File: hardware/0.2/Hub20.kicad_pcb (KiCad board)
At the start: 2 copper layers, 89 x 124 mm, 164 parts, among them J1 USB_C_Receptacle_USB2.0, J2 USB_C_Receptacle_USB2.0, J3 USB_C_Receptacle_USB2.0, J4 USB_C_Receptacle_USB2.0, Q1 DTC123J, Q2 BSS138, SW1 SW_Push, SW10 MX_RGB, SW11 MX_RGB, SW12 MX_RGB, SW13 Rotary_Encoder_Switch, SW14 MX_RGB, SW15 MX_RGB, SW16 MX_RGB, SW17 MX_RGB, SW18 MX_RGB, SW19 MX_RGB, SW2 MX_RGB, SW20 MX_RGB, SW21 MX_RGB, SW22 MX_RGB, SW23 MX_RGB, SW3 MX_RGB, SW4 MX_RGB, SW5 MX_RGB, SW6 MX_RGB, SW7 Rotary_Encoder_Switch, SW8 MX_RGB, SW9 MX_RGB, U1 AP2112K-3.3, U2 USBLC6-2SC6, U3 STM32F072C8Tx, U5 CY7C65632-28LTXCT, U6 USBLC6-2SC6, U7 USBLC6-2SC6, U8 USBLC6-2SC6, Y1 12MHz

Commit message: layout getting close
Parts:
- moved R6 53.2 mm to (163.4, 114.7), turned to 0 degrees
- moved Q2 49.7 mm to (163.4, 112.2), turned to 270 degrees
- moved R5 46.2 mm to (163.4, 109.7), turned to 0 degrees
- moved C9 1.05 mm to (123.8, 70.5), turned to 270 degrees
- moved D24 0.80 mm to (160.9, 43.1)
- moved C38 0.70 mm to (144.5, 86.2)
- moved R10 0.27 mm to (151.9, 51.1)
- moved C59 0.10 mm to (146.7, 42.6)
- moved F3 0.10 mm to (146.5, 44.3)
- moved FB4 0.10 mm to (146.3, 46.0)
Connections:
- C41 pad 1: +3V3 -> +3.3VP
- C56 pad 1: +3V3 -> +3.3VP
- C57 pad 1: +3V3 -> +3.3VP
- FB2 pad 2: +3V3 -> +3.3VP
- R8 pad 2: +3V3 -> +3.3VP
- R9 pad 2: +3V3 -> +3.3VP
- RN3 pad 5: +3V3 -> +3.3VP
- RN3 pad 6: +3V3 -> +3.3VP
- RN3 pad 7: +3V3 -> +3.3VP
- RN3 pad 8: +3V3 -> +3.3VP
- U5 pad 21: +3V3 -> +3.3VP
- U5 pad 28: +3V3 -> +3.3VP
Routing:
- net +3V3: track 22.1 -> 300.4 mm, vias 0 -> 24
- net /C1: track 0.00 -> 190.8 mm, vias 0 -> 8
- net /C2: track 0.00 -> 181.4 mm, vias 0 -> 4
- net /C0: track 0.00 -> 126.5 mm, vias 0 -> 3
- net /C3: track 0.00 -> 117.2 mm, vias 0 -> 7
- net Net-(R1-Pad2): track 0.00 -> 115.7 mm, vias 0 -> 6
- net /R5: track 0.00 -> 107.1 mm, vias 0 -> 4
- net /R0: track 50.9 -> 157.5 mm, vias 0 -> 6
- net /R1: track 0.00 -> 97.7 mm, vias 0 -> 7
- net GND: track 43.9 -> 135.5 mm, vias 28 -> 113
- net /R4: track 0.00 -> 84.5 mm, vias 0 -> 4
- net /R2: track 0.00 -> 74.8 mm, vias 0 -> 5
- net /R3: track 0.00 -> 73.8 mm, vias 0 -> 5
- net /BKLT: track 0.00 -> 72.5 mm, vias 0 -> 2
- net /L_R2: track 0.00 -> 71.1 mm, vias 0 -> 4
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
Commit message: center encoders :/
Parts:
- moved RN1 1.08 mm to (121.6, 56.1)
- moved C50 1.08 mm to (119.0, 56.2)
- moved C52 1.08 mm to (124.2, 56.2)
- moved SW7 0.90 mm to (119.2, 52.7)
- moved C51 0.60 mm to (158.1, 56.3)
- moved C53 0.60 mm to (163.3, 56.3)
- moved RN2 0.60 mm to (160.7, 56.2)
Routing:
- net +3V3: track 300.4 -> 301.8 mm
- net /E1A: track 5.59 -> 4.68 mm
- net /ENC1A_DB: track 50.0 -> 51.0 mm
- net /E2A: track 5.73 -> 4.83 mm
- net /ENC1B_DB: track 50.3 -> 51.2 mm
- net /E2B: track 5.67 -> 4.83 mm
- net /E1B: track 5.53 -> 4.76 mm
- net /ENC2A_DB: track 52.4 -> 53.0 mm
- net /ENC2B_DB: track 52.9 -> 53.5 mm

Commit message: tidy up things
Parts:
- moved D32 0.22 mm to (141.2, 35.0)
- moved R14 0.20 mm to (140.1, 37.5)
- moved JP1 0.20 mm to (142.1, 37.5)
- moved SW1 0.15 mm to (141.2, 41.2)
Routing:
- net +5V: track 115.5 -> 111.4 mm, vias 30 -> 28
- net Net-(C59-Pad1): track 15.5 -> 17.7 mm
- net Net-(D17-Pad2): track 60.1 -> 59.2 mm

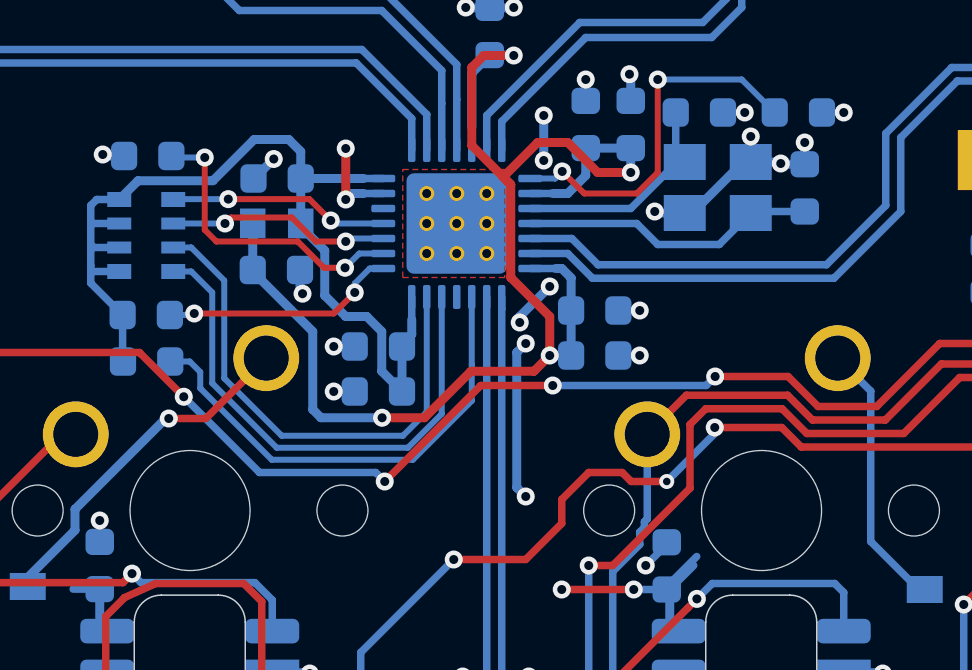
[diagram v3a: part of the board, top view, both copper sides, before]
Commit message: improved ground return under USB hub
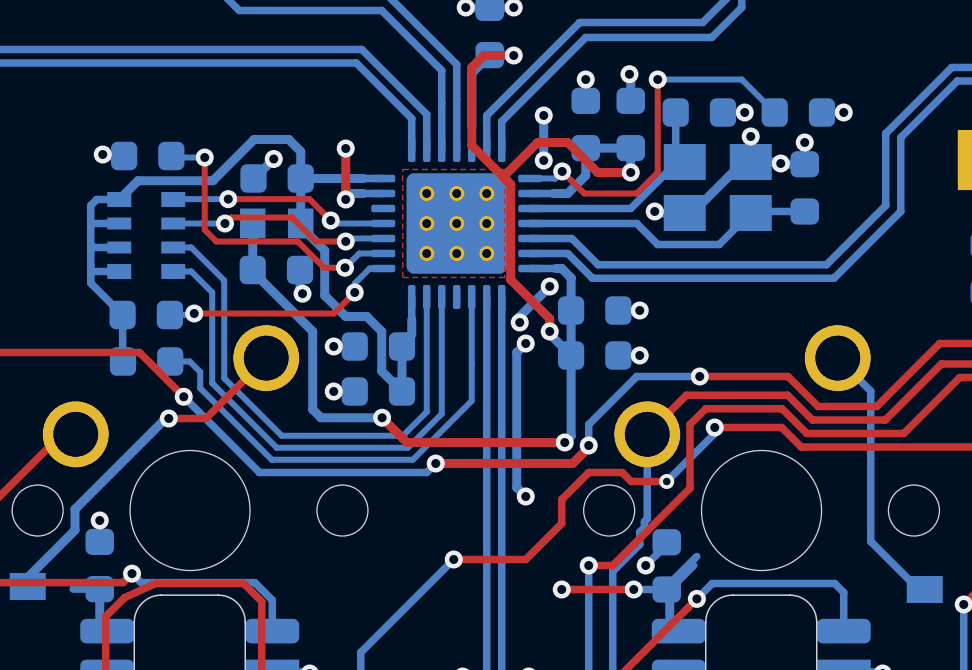
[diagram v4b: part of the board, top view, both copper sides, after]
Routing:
- net +3.3VA: track 48.0 -> 50.5 mm, vias 4 -> 5
